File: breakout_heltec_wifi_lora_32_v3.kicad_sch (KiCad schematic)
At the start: 3 parts, among them J2 Screw_Terminal_01x18, J3 Screw_Terminal_01x18

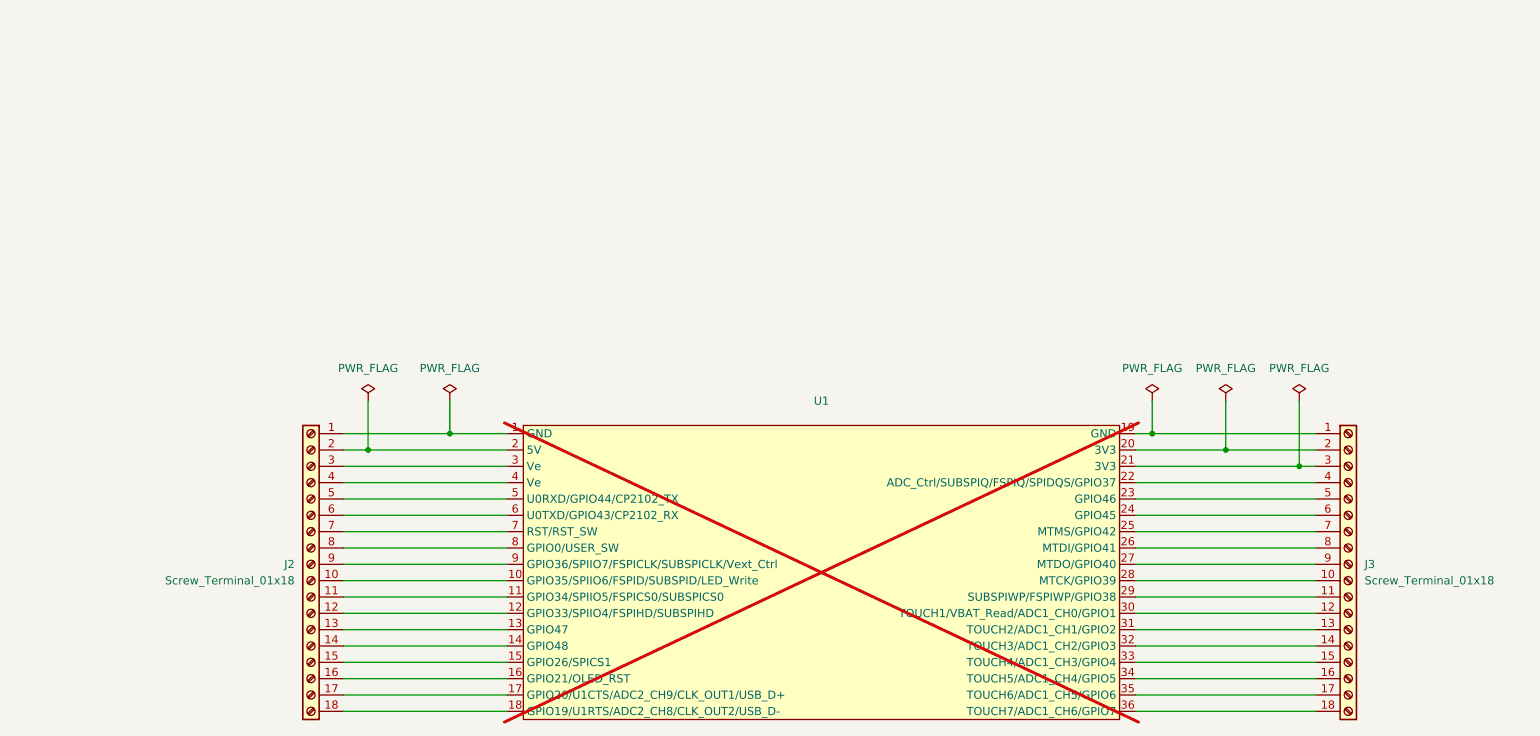
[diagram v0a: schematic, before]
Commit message: feat: Create breakout board PCB layout #3
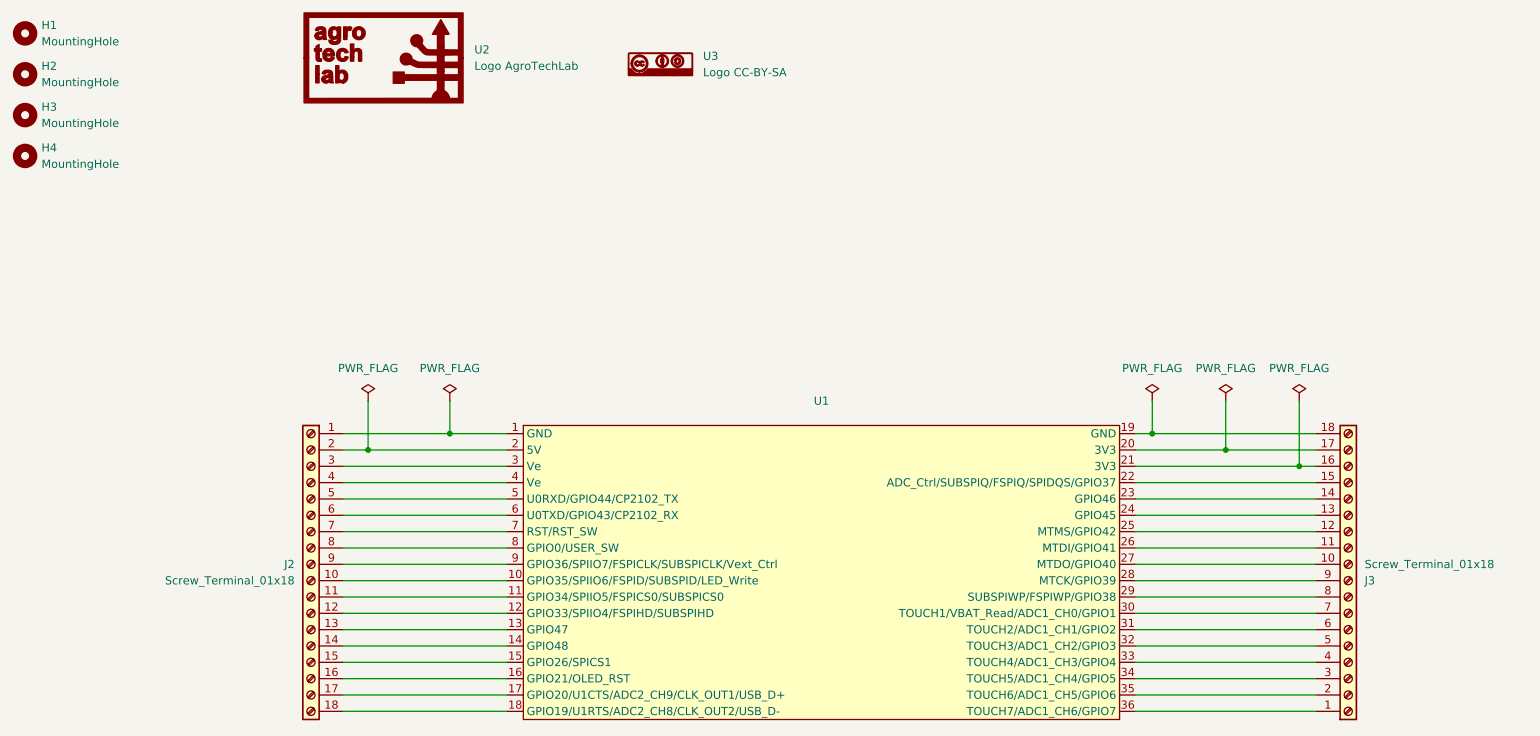
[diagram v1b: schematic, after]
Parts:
- added H1, H2, H3, H4: MountingHole, MountingHole:MountingHole_3.2mm_M3_Pad_Via, symbol Mechanical:MountingHole
- added U2: Logo AgroTechLab, AgroTechLab:Logo AgroTechLab, symbol AgroTechLab:Logo AgroTechLab
- added U3: Logo CC-BY-SA, AgroTechLab:Logo CC-BY-SA, symbol AgroTechLab:Logo CC-BY-SA
- U1: now fitted
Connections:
- net at J3.1 (Pin_1): now also U1.36 (TOUCH7/ADC1_CH6/GPIO7); no longer U1.19 (GND)
- net at U1.20 (3V3): now also J3.17 (Pin_17); no longer J3.2 (Pin_2)
- net at U1.21 (3V3): now also J3.16 (Pin_16); no longer J3.3 (Pin_3)
- net at U1.22 (ADC_Ctrl/SUBSPIQ/FSPIQ/SPIDQS/GPIO37): now also J3.15 (Pin_15); no longer J3.4 (Pin_4)
- net at U1.23 (GPIO46): now also J3.14 (Pin_14); no longer J3.5 (Pin_5)
- net at U1.24 (GPIO45): now also J3.13 (Pin_13); no longer J3.6 (Pin_6)
- net at U1.25 (MTMS/GPIO42): now also J3.12 (Pin_12); no longer J3.7 (Pin_7)
- net at U1.26 (MTDI/GPIO41): now also J3.11 (Pin_11); no longer J3.8 (Pin_8)
- net at U1.27 (MTDO/GPIO40): now also J3.10 (Pin_10); no longer J3.9 (Pin_9)
- net at U1.28 (MTCK/GPIO39): now also J3.9 (Pin_9); no longer J3.10 (Pin_10)
- net at U1.29 (SUBSPIWP/FSPIWP/GPIO38): now also J3.8 (Pin_8); no longer J3.11 (Pin_11)
- net at U1.30 (TOUCH1/VBAT_Read/ADC1_CH0/GPIO1): now also J3.7 (Pin_7); no longer J3.12 (Pin_12)
- net at U1.31 (TOUCH2/ADC1_CH1/GPIO2): now also J3.6 (Pin_6); no longer J3.13 (Pin_13)
- net at U1.32 (TOUCH3/ADC1_CH2/GPIO3): now also J3.5 (Pin_5); no longer J3.14 (Pin_14)
- net at U1.33 (TOUCH4/ADC1_CH3/GPIO4): now also J3.4 (Pin_4); no longer J3.15 (Pin_15)
- net at U1.34 (TOUCH5/ADC1_CH4/GPIO5): now also J3.3 (Pin_3); no longer J3.16 (Pin_16)
- net at U1.35 (TOUCH6/ADC1_CH5/GPIO6): now also J3.2 (Pin_2); no longer J3.17 (Pin_17)
- net at J3.18 (Pin_18): now also U1.19 (GND); no longer U1.36 (TOUCH7/ADC1_CH6/GPIO7)
